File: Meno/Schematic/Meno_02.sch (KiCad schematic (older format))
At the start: 26 parts, among them J1 5077CR-16SMC2, J3 18742, Q1 IRLML6402, U2 FT232RL, U3 LM340MPX-5.0/NOPB, U4 TLV75733PDBVR

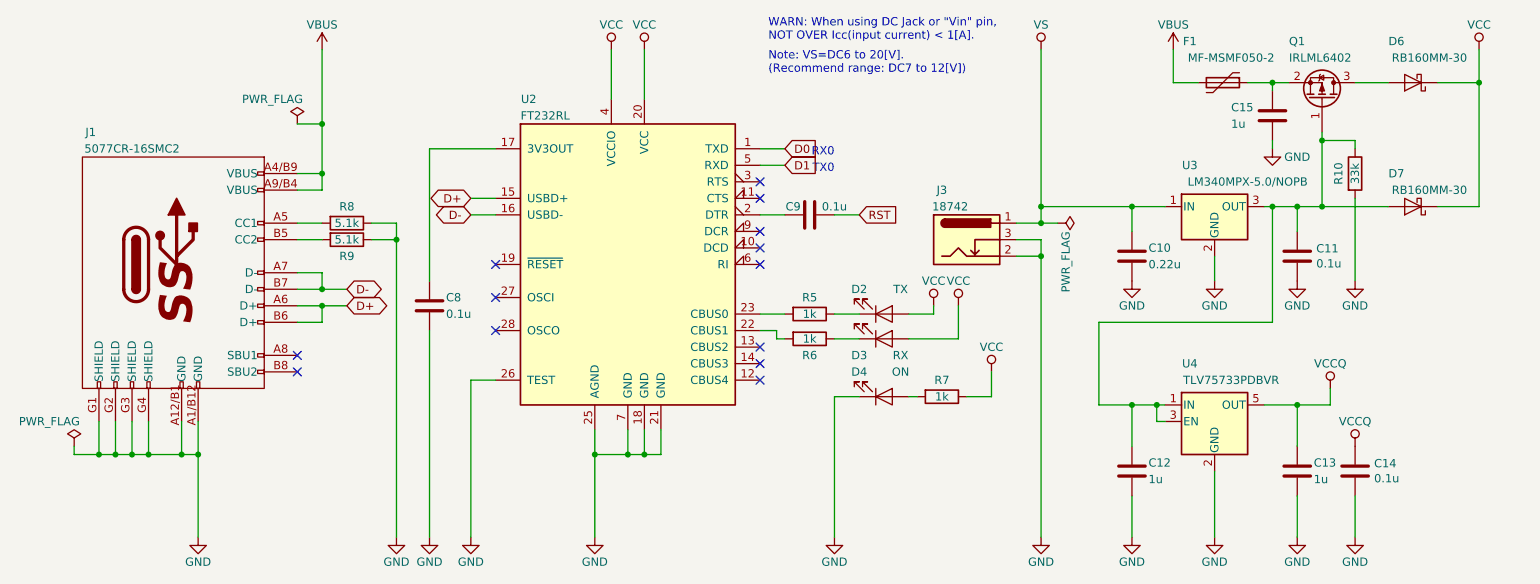
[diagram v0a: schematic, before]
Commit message: ピンソケットの構成を変更
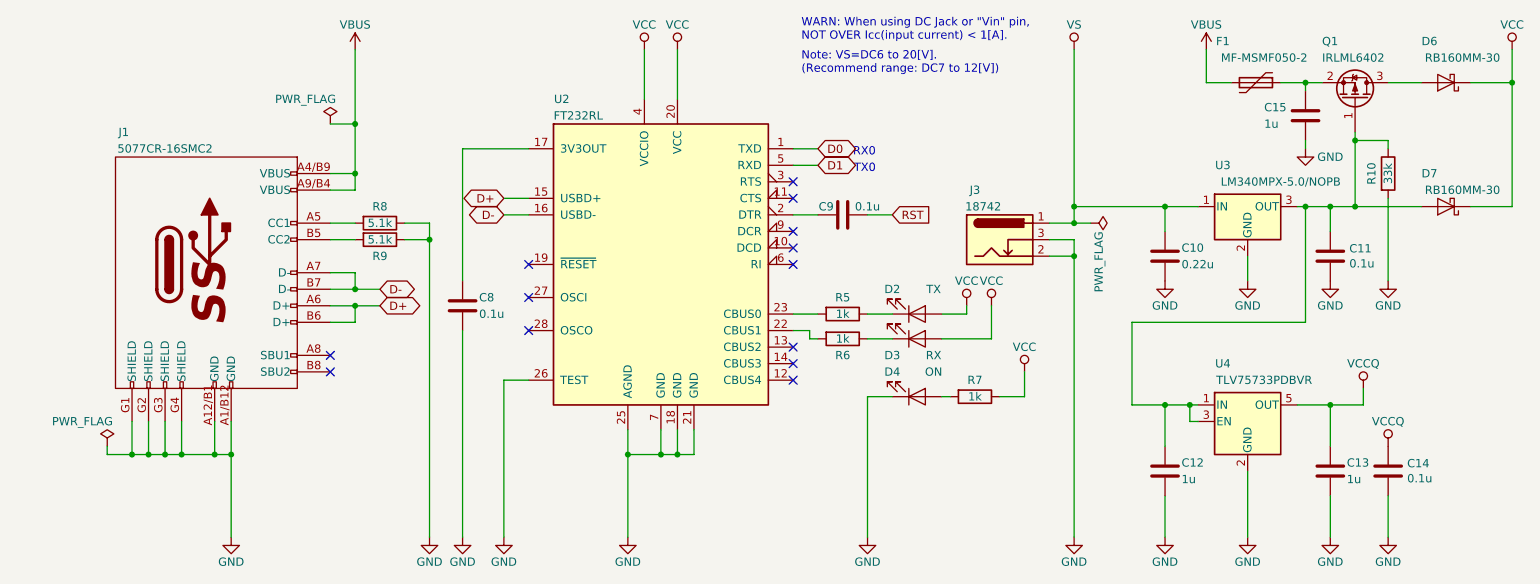
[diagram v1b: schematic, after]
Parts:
- C10, C11, C12, C13, C14, C15, C8, C9: footprint Capacitor_SMD:C_0805_2012Metric -> Capacitor_SMD:C_0805_2012Metric_Pad1.15x1.40mm_HandSolder
- D2, D3, D4: footprint LED_SMD:LED_0805_2012Metric -> LED_SMD:LED_0805_2012Metric_Pad1.15x1.40mm_HandSolder
- D6, D7: footprint Diode_SMD:D_SOD-123F -> SOD123(F)-HandSolder:D_SOD-123
- F1: footprint Fuse:Fuse_1812_4532Metric -> Fuse:Fuse_1812_4532Metric_Pad1.30x3.40mm_HandSolder
- Q1: footprint Package_TO_SOT_SMD:SOT-23 -> Package_TO_SOT_SMD:SOT-23_Handsoldering
- R10, R5, R6, R7, R8, R9: footprint Resistor_SMD:R_0805_2012Metric -> Resistor_SMD:R_0805_2012Metric_Pad1.15x1.40mm_HandSolder
- U4: footprint Package_TO_SOT_SMD:SOT-23-5 -> Package_TO_SOT_SMD:SOT-23-5_HandSoldering
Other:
- moved on the sheet: C10, C11, C12, C13, C14, C15, C8, C9, D2, D3, D4, D6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
